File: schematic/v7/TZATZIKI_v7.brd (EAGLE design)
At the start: 41.1 x 50.1 mm, 31 parts, among them J1 2X20-CHIP-HEADERS2X20CHIP_OFF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, P0 SE11, P1 SE11, P3 SE11, P4 SE11, U2 DS2431P

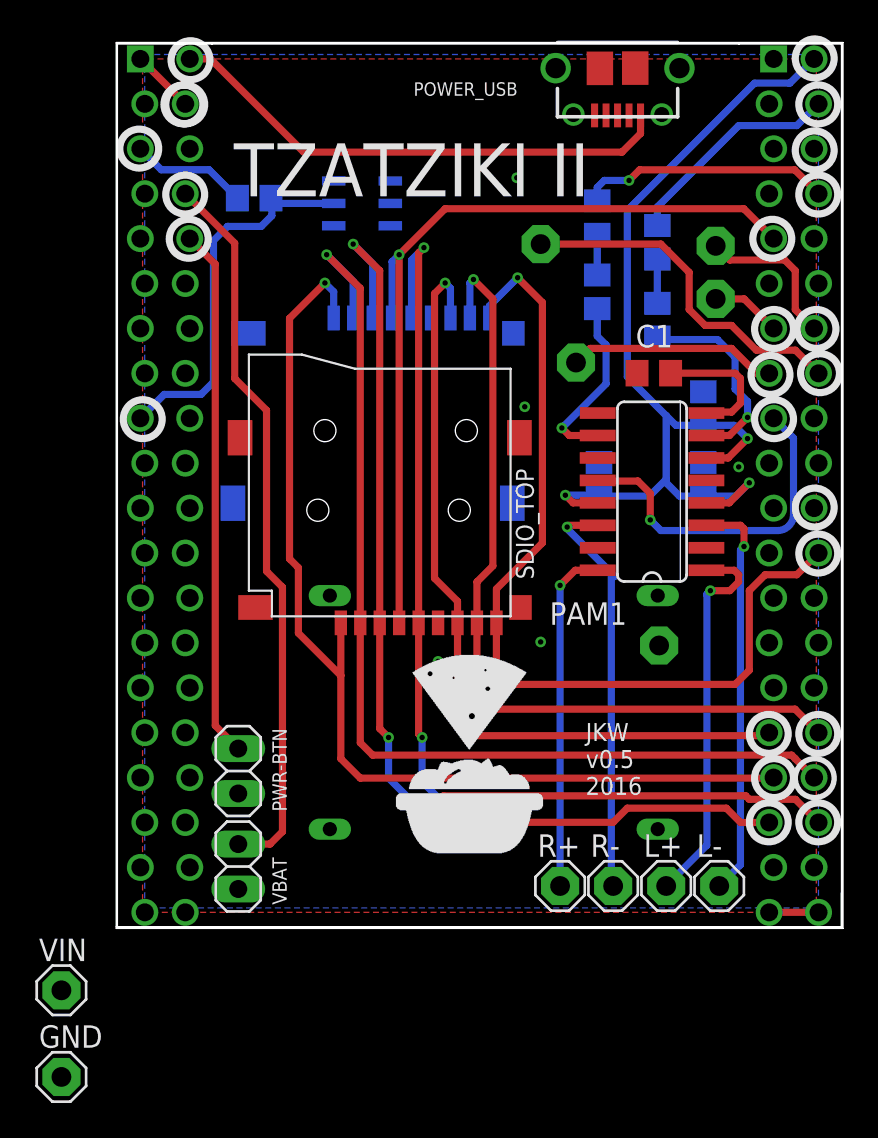
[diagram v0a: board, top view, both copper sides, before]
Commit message: added v7, 0.9mm drills, ordered as 1.0 thick bord
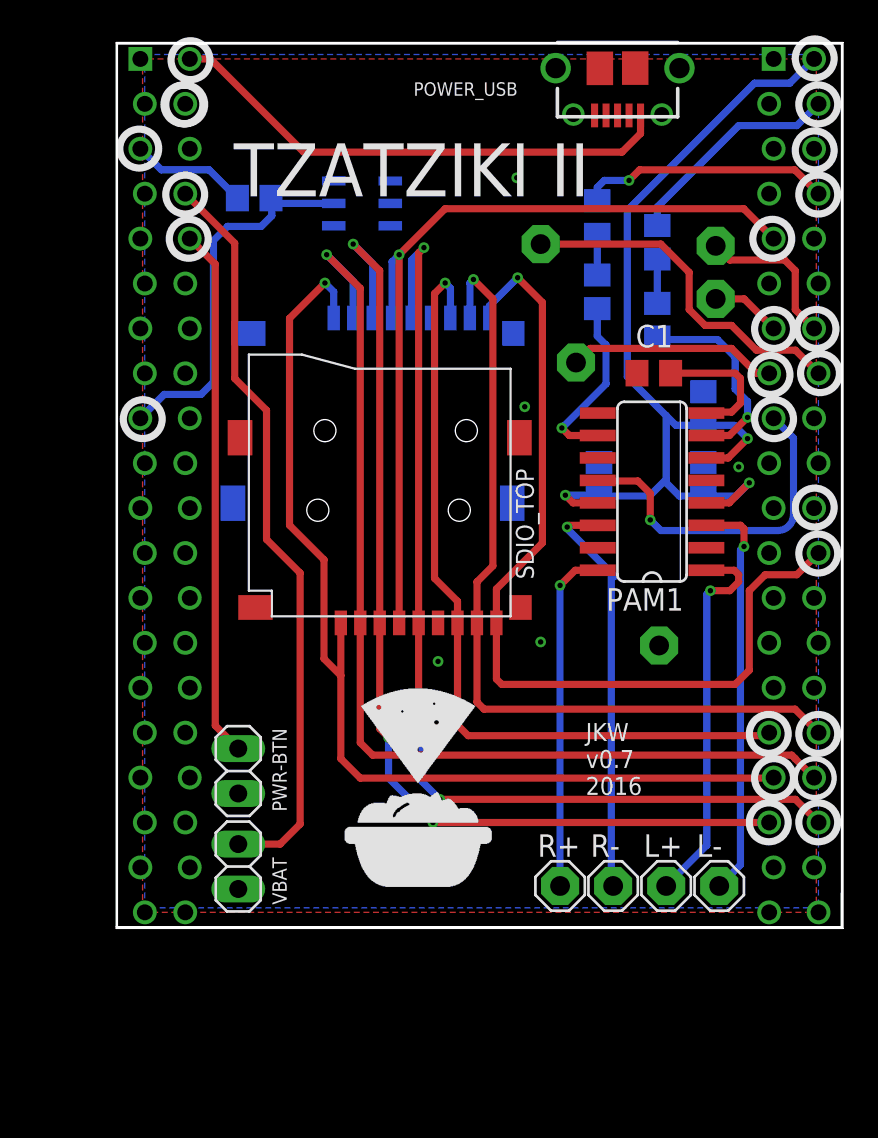
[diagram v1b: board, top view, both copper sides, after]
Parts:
- removed GND99, VIN: SE11, solpad:SE11
- removed U$3: MP1584EN_FRAMELESS, JKW_CHIP:MP1584EN_FRAMELESS
- J1: value 2X20-CHIP-HEADERS2X20CHIP_OFFSET-TH -> 2X20-CHIP
- moved GND 41.7 mm to (38.1, 31.6), flipped to the bottom, turned to 180 degrees
- moved U$1 3.47 mm to (20.3, 17.9)
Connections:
- removed net N$30: U$3.VIN, VIN.MP
- net GND: no longer GND99.MP, U$3.GNDIN, U$3.GNDOUT
- net VOUT: no longer U$3.VOUT
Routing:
- net GND: track 6.39 -> 0.00 mm
- net N$28: track 41.1 -> 42.3 mm
- net N$4: track 58.9 -> 58.2 mm
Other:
- board text added: "JKW v0.7 2016"
- board text removed: "JKW v0.5 2016"
